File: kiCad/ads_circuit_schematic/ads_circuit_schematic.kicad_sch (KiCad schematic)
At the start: 1 part

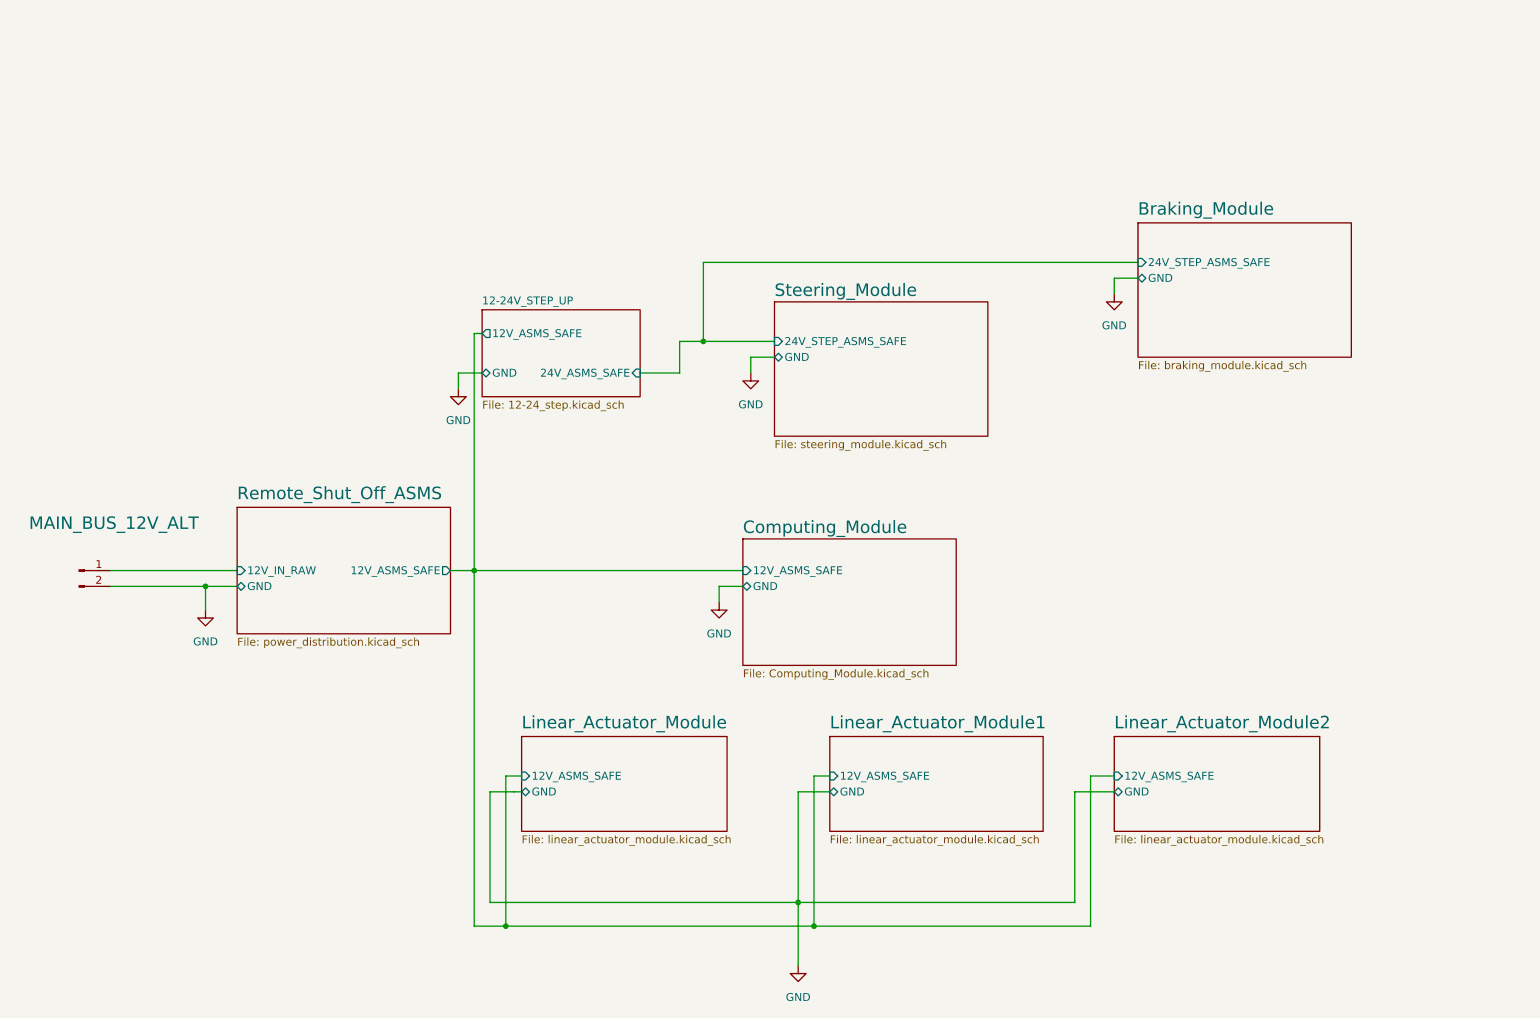
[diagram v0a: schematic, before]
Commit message: Added new symbols for linear actuators, added fuses, added 5V step down
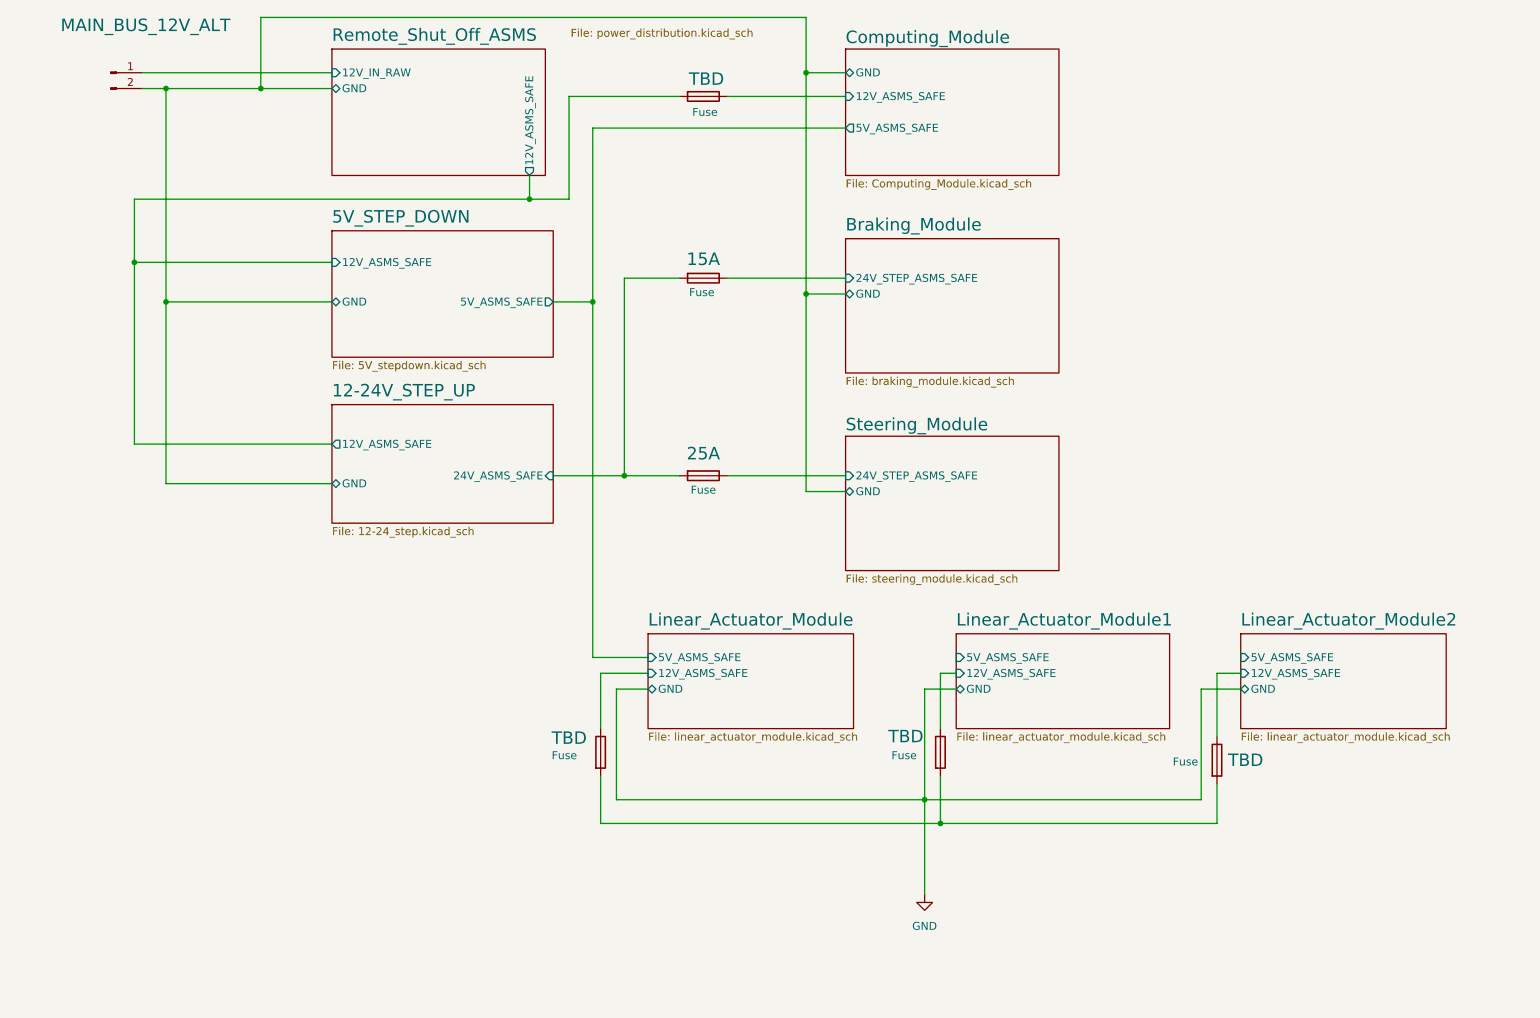
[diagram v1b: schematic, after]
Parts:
- added 15A, 25A, TBD (x4): Fuse, symbol Device:Fuse
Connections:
- net 12-24V_STEP_UP/12V_ASMS_SAFE: now also TBD.2
- net 12-24V_STEP_UP/24V_ASMS_SAFE: now also 15A.2, 25A.2
- net GND: no longer MAIN_BUS_12V_ALT.2 (Pin_2)
- new net: TBD.2, TBD.2, TBD.2
- new net 12-24V_STEP_UP/GND: MAIN_BUS_12V_ALT.2 (Pin_2)
- new net Braking_Module/24V_STEP_ASMS_SAFE: 15A.1
- new net Computing_Module/12V_ASMS_SAFE: TBD.1
- new net Linear_Actuator_Module/12V_ASMS_SAFE: TBD.1
- new net Linear_Actuator_Module1/12V_ASMS_SAFE: TBD.1
- new net Linear_Actuator_Module2/12V_ASMS_SAFE: TBD.1
- new net Steering_Module/24V_STEP_ASMS_SAFE: 25A.1
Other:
- added sheet 5V_STEP_DOWN (5V_stepdown.kicad_sch)
- sheet Computing_Module ports: added 5V_ASMS_SAFE; removed none
- sheet Linear_Actuator_Module ports: added 5V_ASMS_SAFE; removed none
- sheet Linear_Actuator_Module1 ports: added 5V_ASMS_SAFE; removed none
- sheet Linear_Actuator_Module2 ports: added 5V_ASMS_SAFE; removed none
- moved on the sheet: MAIN_BUS_12V_ALT
